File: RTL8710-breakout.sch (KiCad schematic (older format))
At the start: 4 parts, among them IC1 LM1117, U1 RTL01-V1

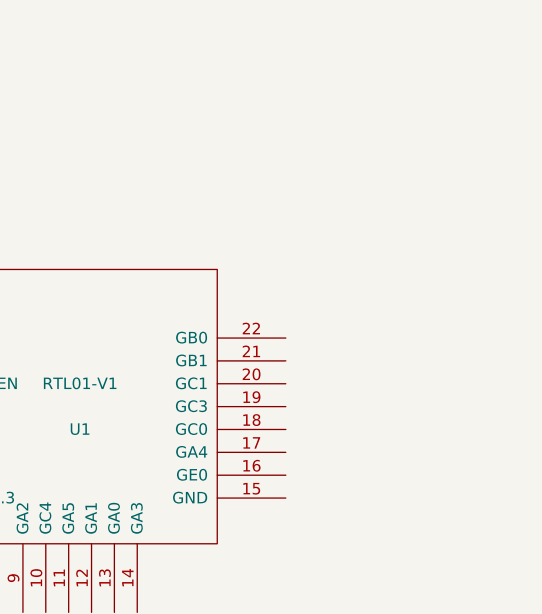
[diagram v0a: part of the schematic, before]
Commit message: add SWD interface
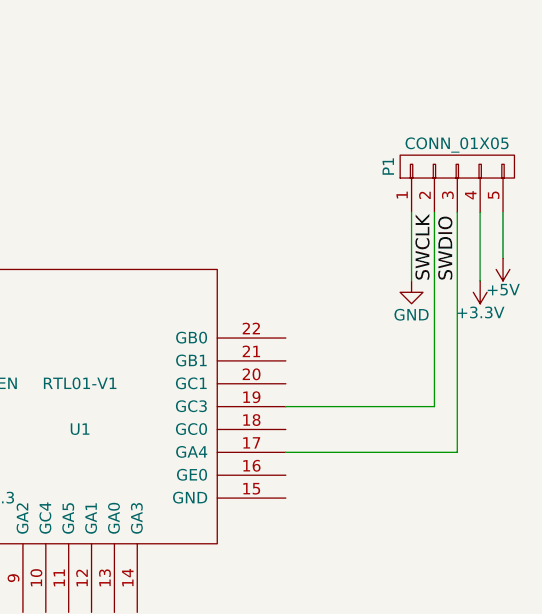
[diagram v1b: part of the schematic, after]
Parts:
- added P1: CONN_01X05, symbol CONN_01X05
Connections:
- net SWDIO: now reaches U1.17 (GA4)
- net SWDIO: now also P1.3 (P3)
- net SWCLK: now reaches U1.19 (GC3)
- net SWCLK: now also P1.2 (P2)
- new net +3V3: P1.4 (P4)
- new net +5V: P1.5 (P5)
- new net GND: P1.1 (P1)
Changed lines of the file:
@@
 	1    0    0    -1
 $EndComp
+$Comp
+L CONN_01X05 P1
+U 1 1 588D0A9E
+P 7000 2400
+F 0 "P1" H 7000 2700 50  0000 C CNN
+F 1 "CONN_01X05" V 7100 2400 50  0000 C CNN
+F 2 "" H 7000 2400 50  0000 C CNN
+F 3 "" H 7000 2400 50  0000 C CNN
+	1    7000 2400
+	0    -1   -1   0
+$EndComp
+Wire Wire Line
+	6250 3450 6900 3450
+Wire Wire Line
+	6900 3450 6900 2600
+Wire Wire Line
+	6250 3650 7000 3650
+Wire Wire Line
+	7000 3650 7000 2600
+Text Label 6900 2900 1    60   ~ 0
+SWCLK
+Text Label 7000 2900 1    60   ~ 0
+SWDIO
+Wire Wire Line
+	7100 2600 7100 2900
+Wire Wire Line
+	6800 2600 6800 2900
+$Comp
+L GND #PWR?
+U 1 1 588D1226
+P 6800 2900
+F 0 "#PWR?" H 6800 2650 50  0001 C CNN
+F 1 "GND" H 6800 2750 50  0000 C CNN
+F 2 "" H 6800 2900 50  0000 C CNN
+F 3 "" H 6800 2900 50  0000 C CNN
+	1    6800 2900
+	1    0    0    -1
+$EndComp
+$Comp
+L +3.3V #PWR?
+U 1 1 588D125D
+P 7100 2900
+F 0 "#PWR?" H 7100 2750 50  0001 C CNN
+F 1 "+3.3V" H 7100 3040 50  0000 C CNN
+F 2 "" H 7100 2900 50  0000 C CNN
+F 3 "" H 7100 2900 50  0000 C CNN
+	1    7100 2900
+	-1   0    0    1
+$EndComp
+Wire Wire Line
+	7200 2600 7200 2800
+$Comp
+L +5V #PWR?
+U 1 1 588D1289
+P 7200 2800
+F 0 "#PWR?" H 7200 2650 50  0001 C CNN
+F 1 "+5V" H 7200 2940 50  0000 C CNN
+F 2 "" H 7200 2800 50  0000 C CNN
+F 3 "" H 7200 2800 50  0000 C CNN
+	1    7200 2800
+	-1   0    0    1
+$EndComp
 $EndSCHEMATC

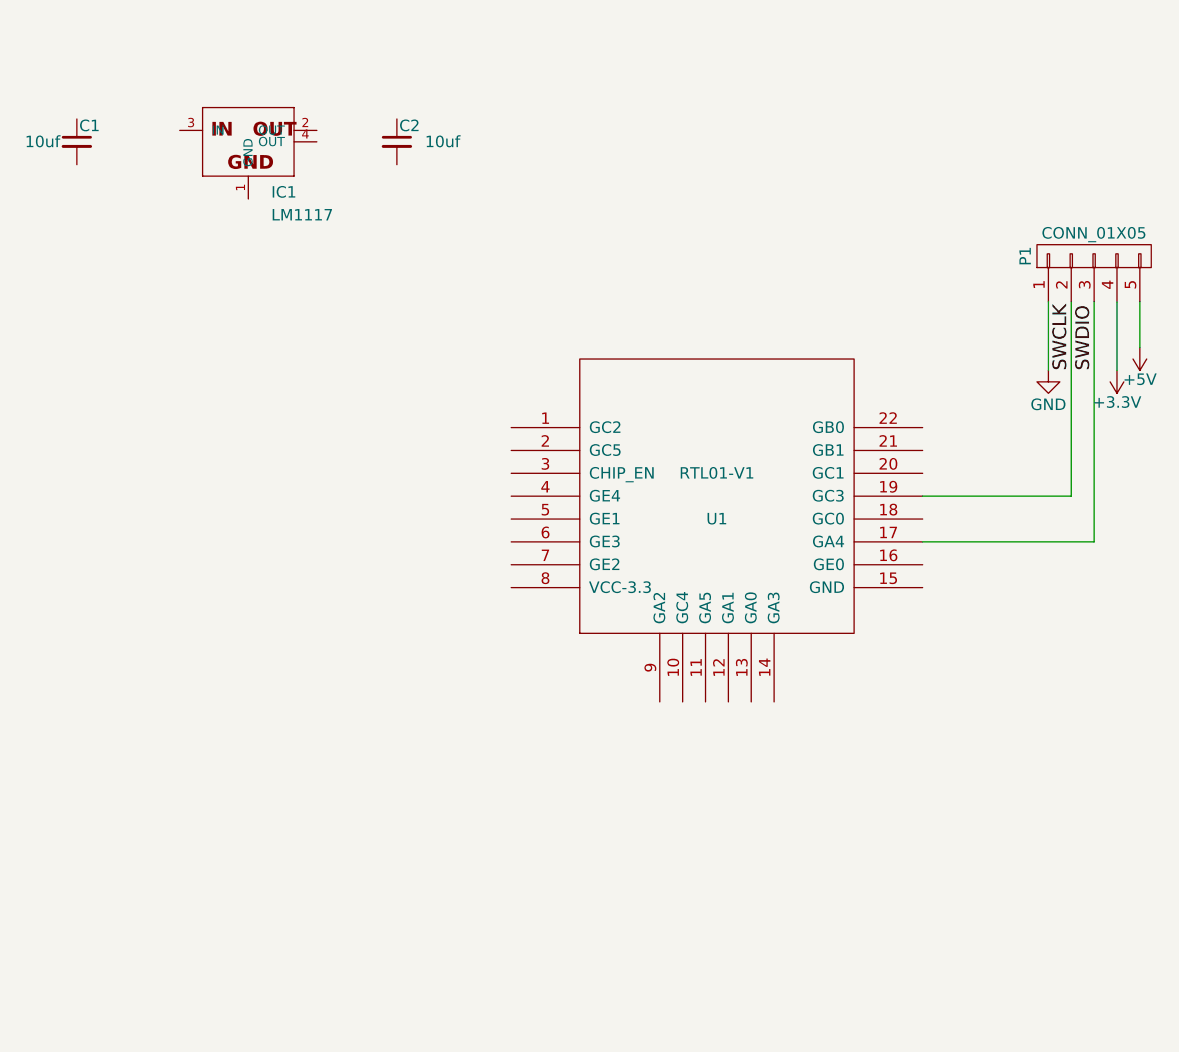
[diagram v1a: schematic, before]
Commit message: add connections to breakout schematic
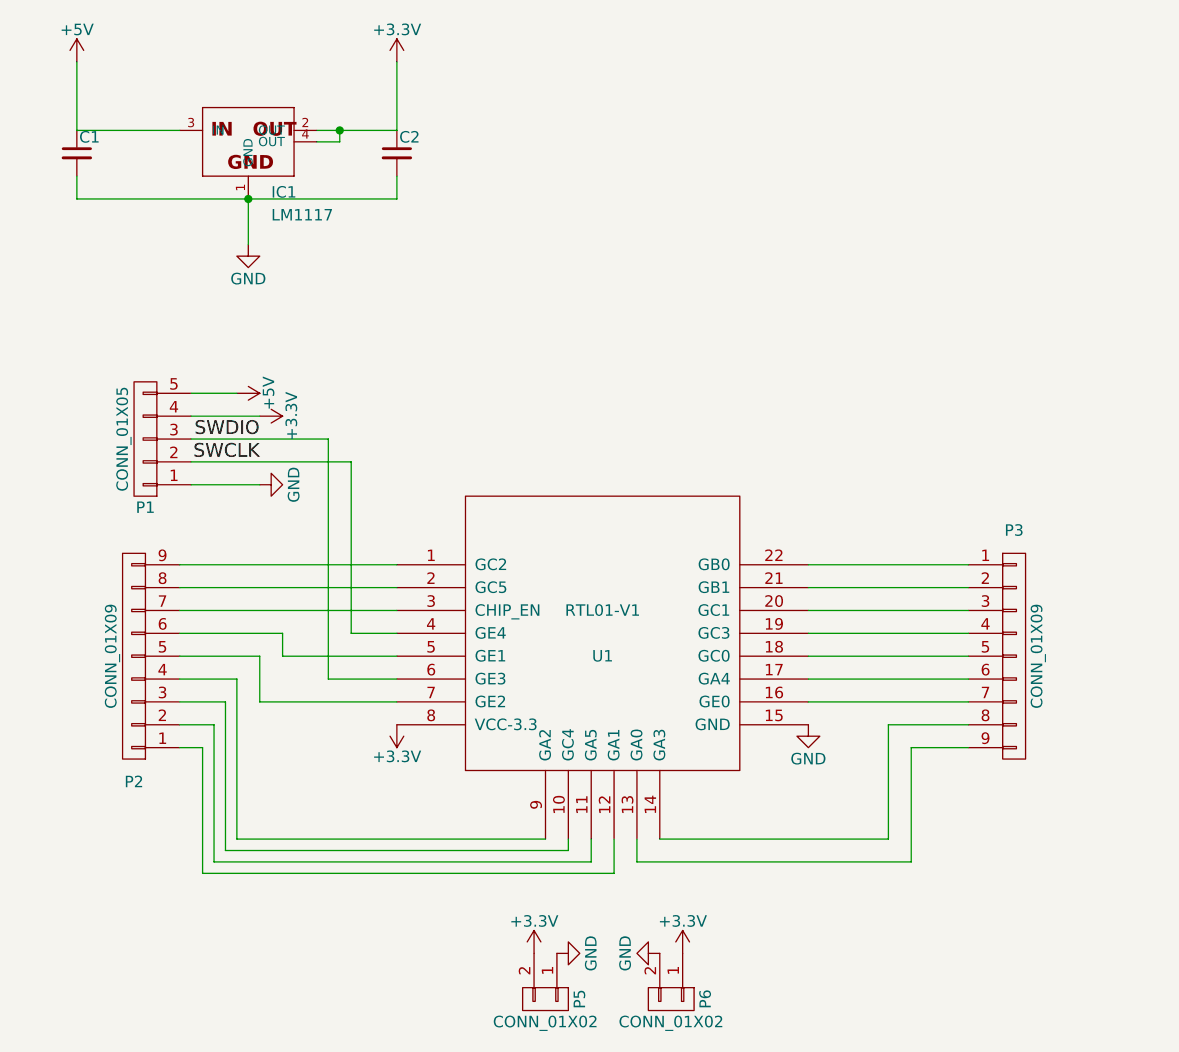
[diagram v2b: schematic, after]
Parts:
- added P2, P3: CONN_01X09, Connectors:CONN_2.54mm_1x9, symbol CONN_01X09
- added P5, P6: CONN_01X02, Connectors:CONN_2.54mm_1x2, symbol CONN_01X02
- C1, C2: value C_Small -> 10uf; footprint 10uf -> Capacitors_SMD:C_0805_HandSoldering
- IC1: footprint (none) -> TO_SOT_Packages_SMD:SOT-223
- P1: footprint (none) -> Connectors:CONN_2.54mm_1x5
- U1: footprint (none) -> RTL8710:RTL01-V1
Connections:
- net +3V3: now also C2.1, IC1.2 (OUT), IC1.4 (OUT), U1.8 (VCC-3.3), P5.2 (P2), P6.1 (P1)
- net +5V: now also C1.1, IC1.3 (IN)
- net GND: now also C1.2, C2.2, IC1.1 (GND), U1.15 (GND), P5.1 (P1), P6.2 (P2)
- net SWCLK: now also U1.4 (GE4); no longer U1.19 (GC3)
- net SWDIO: now also U1.6 (GE3); no longer U1.17 (GA4)
- net at U1.1 (GC2): now also P2.9 (P9)
- net at U1.10 (GC4): now also P2.3 (P3)
- net at U1.11 (GA5): now also P2.2 (P2)
- net at U1.12 (GA1): now also P2.1 (P1)
- net at U1.13 (GA0): now also P3.9 (P9)
- net at U1.14 (GA3): now also P3.8 (P8)
- net at U1.16 (GE0): now also P3.7 (P7)
- net at U1.18 (GC0): now also P3.5 (P5)
- net at U1.2 (GC5): now also P2.8 (P8)
- net at U1.20 (GC1): now also P3.3 (P3)
- net at U1.21 (GB1): now also P3.2 (P2)
- net at U1.22 (GB0): now also P3.1 (P1)
- net at U1.3 (CHIP_EN): now also P2.7 (P7)
- net at U1.5 (GE1): now also P2.6 (P6)
- net at U1.7 (GE2): now also P2.5 (P5)
- net at U1.9 (GA2): now also P2.4 (P4)
- new net: P3.6 (P6), U1.17 (GA4)
- new net: P3.4 (P4), U1.19 (GC3)
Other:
- moved on the sheet: C1, C2, P1

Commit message: finsh pcb layout
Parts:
- added D1: Led_Small, LEDs:LED_0603, symbol Led_Small
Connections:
- net +3V3: now also D1.2 (A)
- net GND: now also D1.1 (K)
- net GC2: now reaches P2.9 (P9), U1.1 (GC2)
- net GC4: now reaches P2.3 (P3), U1.10 (GC4)
- net GA5: now reaches P2.2 (P2), U1.11 (GA5)
- net GA1: now reaches P2.1 (P1), U1.12 (GA1)
- net GA0: now reaches P3.9 (P9), U1.13 (GA0)
- net GA3: now reaches P3.8 (P8), U1.14 (GA3)
- net GE0: now reaches P3.7 (P7), U1.16 (GE0)
- net GA4: now reaches P3.6 (P6), U1.17 (GA4)
- net GC0: now reaches P3.5 (P5), U1.18 (GC0)
- net GC3: now reaches P3.4 (P4), U1.19 (GC3)
- net GC5: now reaches P2.8 (P8), U1.2 (GC5)
- net GC1: now reaches P3.3 (P3), U1.20 (GC1)
- net GB1: now reaches P3.2 (P2), U1.21 (GB1)
- net GB0: now reaches P3.1 (P1), U1.22 (GB0)
- net CHIP_EN: now reaches P2.7 (P7), U1.3 (CHIP_EN)
- net GE1: now reaches P2.6 (P6), U1.5 (GE1)
- net GE2: now reaches P2.5 (P5), U1.7 (GE2)
- net GA2: now reaches P2.4 (P4), U1.9 (GA2)
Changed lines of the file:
@@
 EESchema Schematic File Version 2
+LIBS:RTL8710-breakout-rescue
 LIBS:power
 LIBS:device
@@
 	0    1    1    0
 $EndComp
-$Comp
-L RTL01-V1 U1
-U 1 1 588D83EC
-P 4850 4050
-F 0 "U1" H 4850 3950 50  0000 C CNN
-F 1 "RTL01-V1" H 4850 4150 50  0000 C CNN
-F 2 "RTL8710:RTL01-V1" H 4850 4050 50  0001 C CNN
-F 3 "" H 4850 4050 50  0001 C CNN
-	1    4850 4050
-	1    0    0    -1
-$EndComp
 Text Label 3350 3200 2    60   ~ 0
 SWDIO
@@
 	3950 4150 3450 4150
 Wire Wire Line
-	3350 4350 3950 4350
-Wire Wire Line
 	5750 3750 6450 3750
 Wire Wire Line
@@
 Connection ~ 3700 1850
 Wire Wire Line
-	2550 2150 3950 2150
+	2550 2150 4300 2150
 Wire Wire Line
 	3950 2150 3950 2050
@@
 	3450 4050 3000 4050
 Wire Wire Line
-	3350 4350 3350 4150
-Wire Wire Line
-	3350 4150 3000 4150
+	3000 4150 3400 4150
 Wire Wire Line
 	4700 5000 4700 4950
@@
 	6200 4550 6450 4550
 Wire Wire Line
-	4600 4950 3250 4950
-Wire Wire Line
-	3250 4950 3250 4250
-Wire Wire Line
-	3250 4250 3000 4250
-Wire Wire Line
-	3000 4350 3200 4350
-Wire Wire Line
-	3200 4350 3200 5000
-Wire Wire Line
-	3200 5000 4700 5000
-Wire Wire Line
-	4800 5050 3150 5050
-Wire Wire Line
-	3150 5050 3150 4450
-Wire Wire Line
-	3150 4450 3000 4450
-Wire Wire Line
-	3000 4550 3100 4550
-Wire Wire Line
-	3100 4550 3100 5100
-Wire Wire Line
-	3100 5100 4900 5100
+	3000 4250 3350 4250
+Wire Wire Line
+	3000 4350 3300 4350
+Wire Wire Line
+	3000 4450 3250 4450
+Wire Wire Line
+	3000 4550 3200 4550
 $Comp
 L CONN_01X02 P5
@@
 	0    1    1    0
 $EndComp
+Text Label 3000 3750 0    60   ~ 0
+GC2
+Text Label 3000 3850 0    60   ~ 0
+GC5
+Text Label 3000 3950 0    60   ~ 0
+CHIP_EN
+Text Label 3000 4050 0    60   ~ 0
+GE1
+Wire Wire Line
+	3950 4350 3400 4350
+Wire Wire Line
+	3400 4350 3400 4150
+Wire Wire Line
+	3350 4250 3350 4950
+Wire Wire Line
+	3350 4950 4600 4950
+Wire Wire Line
+	4700 5000 3300 5000
+Wire Wire Line
+	3300 5000 3300 4350
+Wire Wire Line
+	3250 4450 3250 5050
+Wire Wire Line
+	3250 5050 4800 5050
+Wire Wire Line
+	3200 4550 3200 5100
+Wire Wire Line
+	3200 5100 4900 5100
+Text Label 3000 4150 0    60   ~ 0
+GE2
+Text Label 3000 4250 0    60   ~ 0
+GA2
+Text Label 3000 4350 0    60   ~ 0
+GC4
+Text Label 3000 4450 0    60   ~ 0
+GA5
+Text Label 3000 4550 0    60   ~ 0
+GA1
+Text Label 6250 3750 0    60   ~ 0
+GB0
+Text Label 6250 3850 0    60   ~ 0
+GB1
+Text Label 6250 3950 0    60   ~ 0
+GC1
+Text Label 6250 4050 0    60   ~ 0
+GC3
+Text Label 6250 4150 0    60   ~ 0
+GC0
+Text Label 6250 4250 0    60   ~ 0
+GA4
+Text Label 6250 4350 0    60   ~ 0
+GE0
+Text Label 6250 4450 0    60   ~ 0
+GA3
+Text Label 6250 4550 0    60   ~ 0
+GA0
+$Comp
+L Led_Small D1
+U 1 1 5890261F
+P 4300 1900
+F 0 "D1" H 4250 2025 50  0000 L CNN
+F 1 "Led_Small" H 4125 1800 50  0000 L CNN
+F 2 "LEDs:LED_0603" V 4300 1900 50  0001 C CNN
+F 3 "" V 4300 1900 50  0000 C CNN
+	1    4300 1900
+	0    -1   -1   0
+$EndComp
+Wire Wire Line
+	4300 1800 4300 1650
+Wire Wire Line
+	4300 1650 3950 1650
+Connection ~ 3950 1650
+Wire Wire Line
+	4300 2150 4300 2000
+Connection ~ 3950 2150
+$Comp
+L RTL01-V1 U1
+U 1 1 58903084
+P 4850 4050
+F 0 "U1" H 4850 3950 50  0000 C CNN
+F 1 "RTL01-V1" H 4850 4150 50  0000 C CNN
+F 2 "RTL8710:RTL01-V1" H 4850 4050 50  0001 C CNN
+F 3 "" H 4850 4050 50  0001 C CNN
+	1    4850 4050
+	1    0    0    -1
+$EndComp
 $EndSCHEMATC
